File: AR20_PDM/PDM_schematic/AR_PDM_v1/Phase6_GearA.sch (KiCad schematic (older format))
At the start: 15 parts, among them Q1 BTS50025-1TAD, U1 INA233

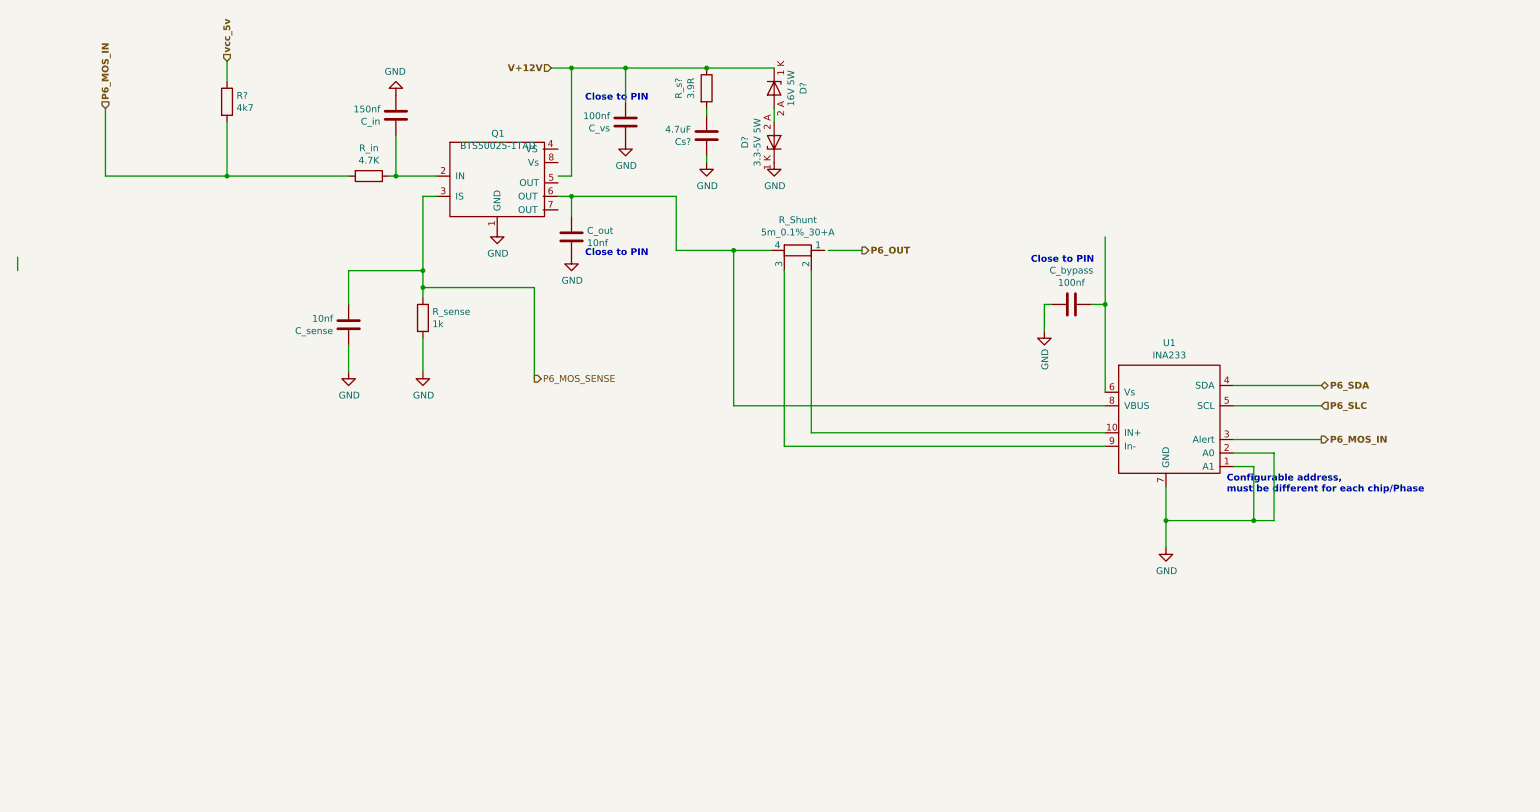
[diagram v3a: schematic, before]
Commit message: Fixed issues, controlled components, BOM, see discription
- added acm symbol
- fixed wrongly faced P-mosfets
- I/O expander now sinks led instead of source
- Bill of material mostly done
- Correct address for INA233 chips.
- Now 4 diodes serves as flyback for all mosfets
- Corrected naming scheme for compmonents (everything is not fixed yet)
- Fixed some labels
- altso some minor changes
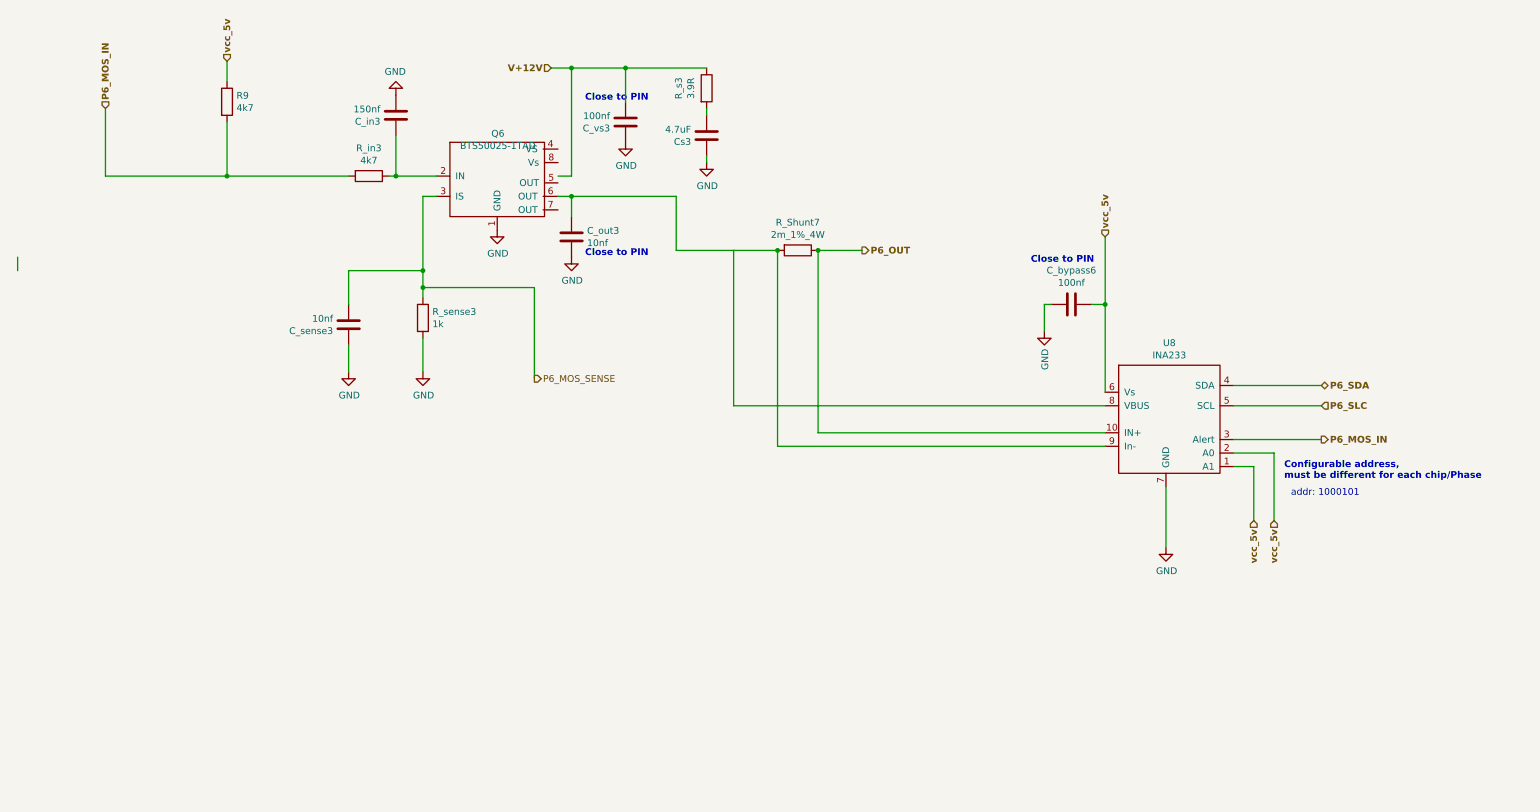
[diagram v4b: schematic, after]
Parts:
- removed C_bypass, C_vs: 100nf, symbol AR20_PDM_v1-rescue:C-Device
- removed C_in: 150nf, symbol AR20_PDM_v1-rescue:C-Device
- removed C_sense: 10nf, symbol AR20_PDM_v1-rescue:C-Device
- removed Cs?: 4.7uF, symbol AR20_PDM_v1-rescue:C-Device
- removed D?: 3.3-5V 5W, symbol AR20_PDM_v1-rescue:D_Zener-Device
- removed D?: 16V 5W, symbol AR20_PDM_v1-rescue:D_Zener-Device
- removed R_Shunt: 5m_0.1%_30+A, symbol AR20_PDM_v1-rescue:R_Shunt-Device
- removed R_in: 4.7K, symbol AR20_PDM_v1-rescue:R-Device
- removed R_s?: 3.9R, symbol AR20_PDM_v1-rescue:R-Device
- removed R_sense: 1k, symbol AR20_PDM_v1-rescue:R-Device
- removed U1: INA233, symbol AR20_PDM_v1-rescue:INA233
- added C_bypass6, C_vs3: 100nf, Capacitor_SMD:C_0603_1608Metric, symbol AR20_PDM_v1-rescue:C-Device
- added C_in3: 150nf, Capacitor_SMD:C_0603_1608Metric, symbol AR20_PDM_v1-rescue:C-Device
- added C_sense3: 10nf, Capacitor_SMD:C_0603_1608Metric, symbol AR20_PDM_v1-rescue:C-Device
- added Cs3: 4.7uF, Capacitor_SMD:C_1206_3216Metric, symbol AR20_PDM_v1-rescue:C-Device
- added R_Shunt7: 2m_1%_4W, symbol AR20_PDM_v1-rescue:R-Device
- added R_in3: 4k7, symbol AR20_PDM_v1-rescue:R-Device
- added R_s3: 3.9R, symbol AR20_PDM_v1-rescue:R-Device
- added R_sense3: 1k, symbol AR20_PDM_v1-rescue:R-Device
- added U8: INA233, symbol AR20_PDM_v1-rescue:INA233
- C_out3: renamed from C_out; footprint (none) -> Capacitor_SMD:C_0603_1608Metric
- gave numbers to parts that had none: 1
- renumbered Q1 to Q6
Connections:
- wire segments 58 -> 53
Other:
- note added: "addr: 1000101"

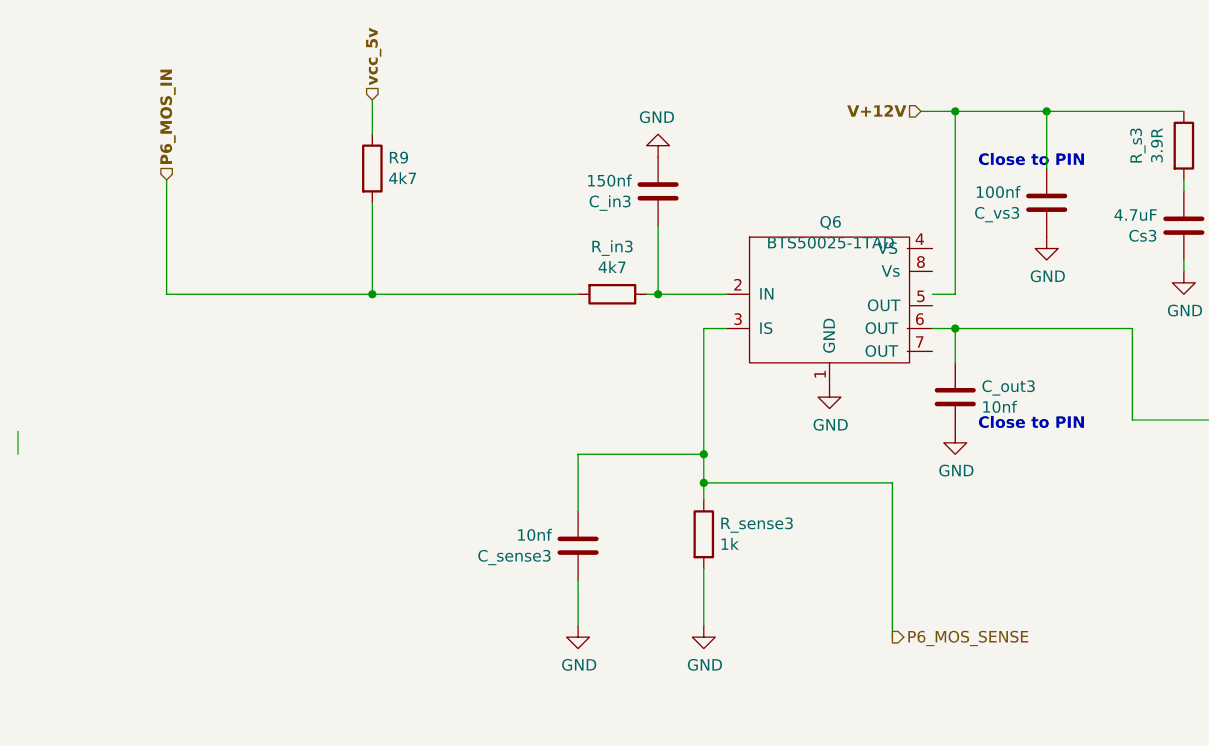
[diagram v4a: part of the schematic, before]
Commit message: PCB design, and issue fixing, work in progress
- Error fixed: Mux mosfet resistor change to ground
- Open drain output added on phase 6, for engine blipping purpose
- Most of pcb symbols and footprints are finished, including main connector
- PCB is change from 1oz to 2oz copper layer, for easier routing.
- Basic Draft of pcb is done, for now.
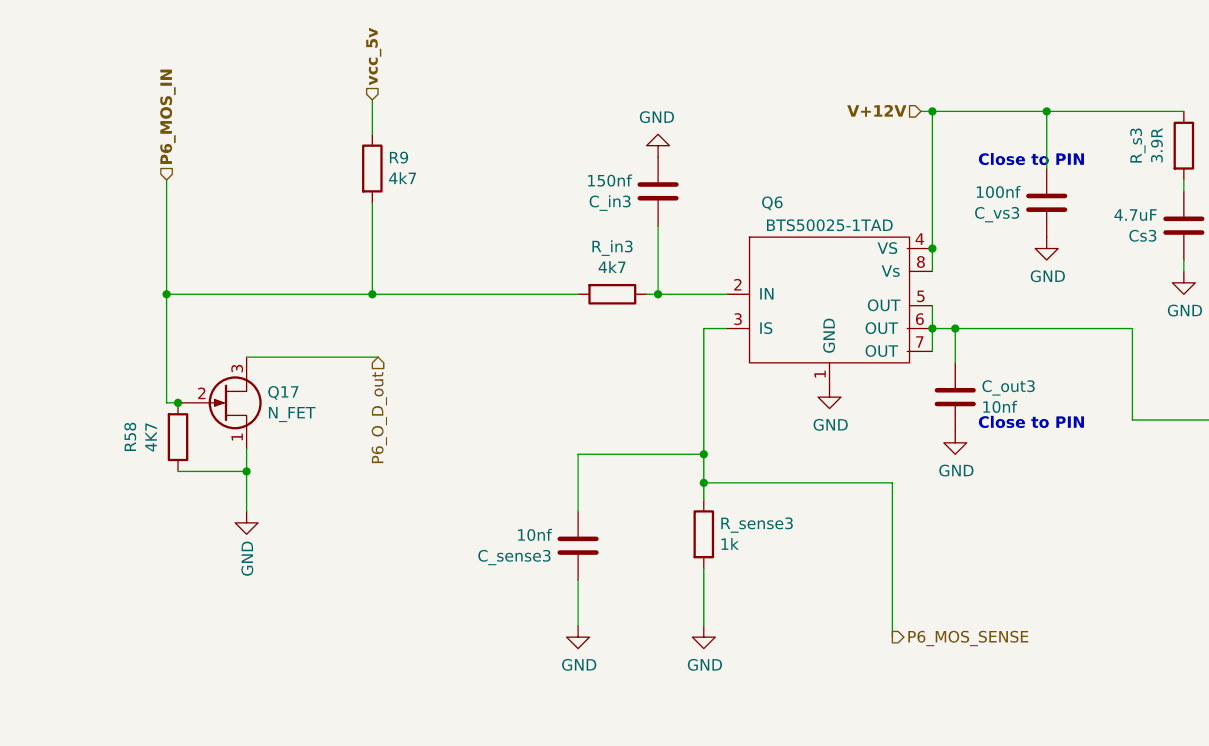
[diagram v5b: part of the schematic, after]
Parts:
- added Q17: N_FET, Package_TO_SOT_SMD:SOT-23, symbol Device:Q_NJFET_DGS
- added R58: 4K7, Resistor_SMD:R_0603_1608Metric, symbol AR20_PDM_v1-rescue:R-Device
- Q6: footprint (none) -> AR_PDM_v1:BTS500xx
- R9, R_in3, R_s3, R_sense3: footprint (none) -> Resistor_SMD:R_0603_1608Metric
- R_Shunt7: footprint (none) -> Resistor_SMD:R_2512_6332Metric
- U8: footprint (none) -> AR_PDM_v1:INA233
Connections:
- net labels added: P6_O_D_out
- wire segments 53 -> 60
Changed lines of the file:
@@
 F 0 "R_in3" V 3093 2400 50  0000 C CNN
 F 1 "4k7" V 3184 2400 50  0000 C CNN
-F 2 "" V 3230 2400 50  0001 C CNN
+F 2 "Resistor_SMD:R_0603_1608Metric" V 3230 2400 50  0001 C CNN
 F 3 "~" H 3300 2400 50  0001 C CNN
 	1    3300 2400
@@
 F 0 "R9" H 2320 1896 50  0000 L CNN
 F 1 "4k7" H 2320 1805 50  0000 L CNN
-F 2 "" V 2180 1850 50  0001 C CNN
+F 2 "Resistor_SMD:R_0603_1608Metric" V 2180 1850 50  0001 C CNN
 F 3 "~" H 2250 1850 50  0001 C CNN
 	1    2250 1850
@@
 AR Path="/5E0FDCCC/5DA8B874" Ref="Q6"  Part="1"
 AR Path="/5E10174B/5DA8B874" Ref="Q?"  Part="1"
-F 0 "Q6" H 4255 3215 50  0000 C CNN
-F 1 "BTS50025-1TAD" H 4255 3124 50  0000 C CNN
-F 2 "" H 4250 2650 50  0001 C CNN
+F 0 "Q6" H 4000 3300 50  0000 C CNN
+F 1 "BTS50025-1TAD" H 4250 3200 50  0000 C CNN
+F 2 "AR_PDM_v1:BTS500xx" H 4250 2650 50  0001 C CNN
 F 3 "" H 4250 2650 50  0001 C CNN
 	1    4250 2650
@@
 F 0 "U8" H 9225 4465 50  0000 C CNN
 F 1 "INA233" H 9225 4374 50  0000 C CNN
-F 2 "" H 9200 4050 50  0001 C CNN
+F 2 "AR_PDM_v1:INA233" H 9200 4050 50  0001 C CNN
 F 3 "" H 9200 4050 50  0001 C CNN
 	1    9200 4050
@@
 Wire Wire Line
 	3700 3100 3700 3225
-Wire Wire Line
-	4700 2400 4800 2400
-Wire Wire Line
-	4800 2400 4800 1600
-Wire Wire Line
-	4800 1600 4650 1600
 Text HLabel 2250 1550 1    50   Input ~ 10
 vcc_5v
@@
 F 0 "R_s3" V 5593 1750 50  0000 C CNN
 F 1 "3.9R" V 5684 1750 50  0000 C CNN
-F 2 "" V 5730 1750 50  0001 C CNN
+F 2 "Resistor_SMD:R_0603_1608Metric" V 5730 1750 50  0001 C CNN
 F 3 "~" H 5800 1750 50  0001 C CNN
 	1    5800 1750
@@
 Wire Wire Line
 	5200 1600 5800 1600
-Wire Wire Line
-	4800 1600 5200 1600
-Connection ~ 4800 1600
 Connection ~ 5200 1600
 Text HLabel 1350 1900 1    50   Input ~ 10
@@
 Wire Wire Line
 	1350 1900 1350 2400
-Wire Wire Line
-	1350 2400 2250 2400
-Wire Wire Line
-	700  3000 700  3100
 Wire Wire Line
 	10000 4450 10000 4950
@@
 F 0 "R_sense3" H 3770 3496 50  0000 L CNN
 F 1 "1k" H 3770 3405 50  0000 L CNN
-F 2 "" V 3630 3450 50  0001 C CNN
+F 2 "Resistor_SMD:R_0603_1608Metric" V 3630 3450 50  0001 C CNN
 F 3 "~" H 3700 3450 50  0001 C CNN
 	1    3700 3450
@@
 F 0 "R_Shunt7" V 6268 2950 50  0000 C CNN
 F 1 "2m_1%_4W" V 6359 2950 50  0000 C CNN
-F 2 "" V 6405 2950 50  0001 C CNN
+F 2 "Resistor_SMD:R_2512_6332Metric" V 6405 2950 50  0001 C CNN
 F 3 "~" H 6475 2950 50  0001 C CNN
 	1    6475 2950
@@
 Text HLabel 10000 4950 3    50   Input ~ 10
 vcc_5v
+Wire Wire Line
+	4650 1600 4700 1600
+Wire Wire Line
+	4700 2650 4700 2550
+Connection ~ 4700 2550
+Wire Wire Line
+	4700 2450 4700 2550
+Wire Wire Line
+	4700 2300 4700 2200
+Wire Wire Line
+	4700 2200 4700 1600
+Connection ~ 4700 2200
+Connection ~ 4700 1600
+Wire Wire Line
+	4700 1600 5200 1600
+Text HLabel 2275 2675 3    50   Input ~ 0
+P6_O_D_out
+Wire Wire Line
+	1700 3175 1700 3350
+Connection ~ 1700 3175
+Wire Wire Line
+	1700 3075 1700 3175
+Wire Wire Line
+	1400 3175 1700 3175
+Connection ~ 1400 2875
+Wire Wire Line
+	1400 2875 1350 2875
+$Comp
+L AR20_PDM_v1-rescue:R-Device R_s?
+U 1 1 5E25DA34
+P 1400 3025
+AR Path="/5DA89415/5E25DA34" Ref="R_s?"  Part="1"
+AR Path="/5DA8920B/5E25DA34" Ref="R_s?"  Part="1"
+AR Path="/5E2546F2/5E25DA34" Ref="R_s?"  Part="1"
+AR Path="/5E0FDCCC/5E25DA34" Ref="R58"  Part="1"
+F 0 "R58" V 1193 3025 50  0000 C CNN
+F 1 "4K7" V 1284 3025 50  0000 C CNN
+F 2 "Resistor_SMD:R_0603_1608Metric" V 1330 3025 50  0001 C CNN
+F 3 "~" H 1400 3025 50  0001 C CNN
+	1    1400 3025
+	1    0    0    1
+$EndComp
+$Comp
+L Device:Q_NJFET_DGS Q?
+U 1 1 5E25DA2E
+P 1600 2875
+AR Path="/5DA8920B/5E25DA2E" Ref="Q?"  Part="1"
+AR Path="/5E2546F2/5E25DA2E" Ref="Q?"  Part="1"
+AR Path="/5E0FDCCC/5E25DA2E" Ref="Q17"  Part="1"
+F 0 "Q17" H 1791 2829 50  0000 L CNN
+F 1 "N_FET" H 1791 2920 50  0000 L CNN
+F 2 "Package_TO_SOT_SMD:SOT-23" H 1800 2975 50  0001 C CNN
+F 3 "~" H 1600 2875 50  0001 C CNN
+	1    1600 2875
+	1    0    0    1
+$EndComp
+Wire Wire Line
+	1700 2675 2275 2675
+$Comp
+L AR20_PDM_v1-rescue:GND-power #PWR?
+U 1 1 5E27870A
+P 1700 3350
+AR Path="/5DA89415/5E27870A" Ref="#PWR?"  Part="1"
+AR Path="/5DEB10A1/5E27870A" Ref="#PWR?"  Part="1"
+AR Path="/5DEB20EA/5E27870A" Ref="#PWR?"  Part="1"
+AR Path="/5E0E4725/5E27870A" Ref="#PWR?"  Part="1"
+AR Path="/5E0E4A93/5E27870A" Ref="#PWR?"  Part="1"
+AR Path="/5E0E4EB5/5E27870A" Ref="#PWR?"  Part="1"
+AR Path="/5E0E5304/5E27870A" Ref="#PWR?"  Part="1"
+AR Path="/5E0E594B/5E27870A" Ref="#PWR?"  Part="1"
+AR Path="/5E0E607C/5E27870A" Ref="#PWR?"  Part="1"
+AR Path="/5E0FB5C8/5E27870A" Ref="#PWR?"  Part="1"
+AR Path="/5E0FBBBD/5E27870A" Ref="#PWR?"  Part="1"
+AR Path="/5E0FC3A2/5E27870A" Ref="#PWR?"  Part="1"
+AR Path="/5E0FCFDC/5E27870A" Ref="#PWR?"  Part="1"
+AR Path="/5E0FDCCC/5E27870A" Ref="#PWR0124"  Part="1"
+AR Path="/5E10174B/5E27870A" Ref="#PWR?"  Part="1"
+AR Path="/5E1AEC18/5E27870A" Ref="#PWR?"  Part="1"
+F 0 "#PWR0124" H 1700 3100 50  0001 C CNN
+F 1 "GND" V 1705 3222 50  0000 R CNN
+F 2 "" H 1700 3350 50  0001 C CNN
+F 3 "" H 1700 3350 50  0001 C CNN
+	1    1700 3350
+	1    0    0    -1
+$EndComp
+Wire Wire Line
+	1350 2400 2250 2400
+Wire Wire Line
+	1350 2400 1350 2875
+Connection ~ 1350 2400
 $EndSCHEMATC

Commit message: PCB Design, Work in progress
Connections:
- net P6_Shunt: now reaches C_out3.1, Q6.5 (OUT), Q6.6 (OUT), Q6.7 (OUT), R_Shunt7.2, U8.8 (VBUS), U8.9 (In-)
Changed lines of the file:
@@
 $Descr A4 11693 8268
 encoding utf-8
-Sheet 7 13
+Sheet 6 13
 Title ""
 Date ""
@@
 	1350 2400 1350 2875
 Connection ~ 1350 2400
+Wire Wire Line
+	6000 2950 6000 2825
+Text HLabel 6000 2825 1    50   Input ~ 0
+P6_Shunt
+Connection ~ 6000 2950
 $EndSCHEMATC
